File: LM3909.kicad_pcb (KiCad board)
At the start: 2 copper layers, 19 parts, among them J1 Conn_01x04, J2 Conn_01x04, Q1 MMBT3904, Q2A1 MMBT3906, Q2B1 MMBT3906, Q3 MMBT3904, Q4 MMBT3904

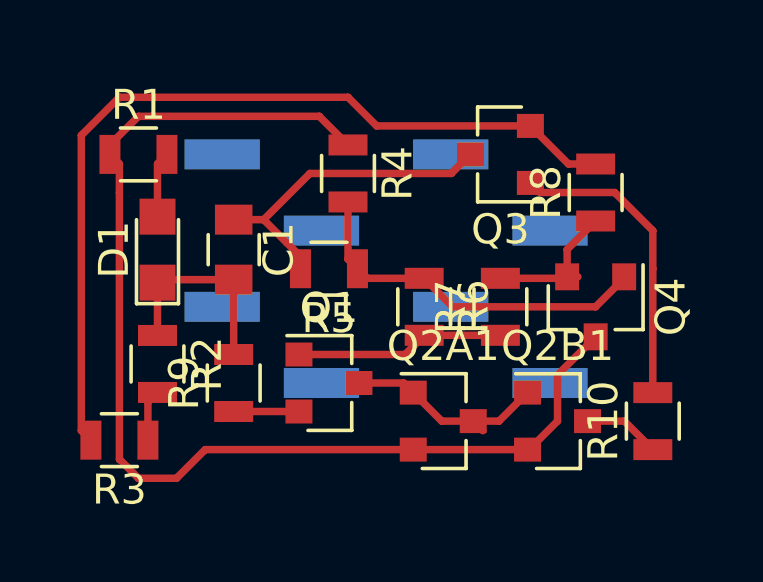
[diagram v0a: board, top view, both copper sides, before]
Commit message: connect the 6 pins on the bottom layer
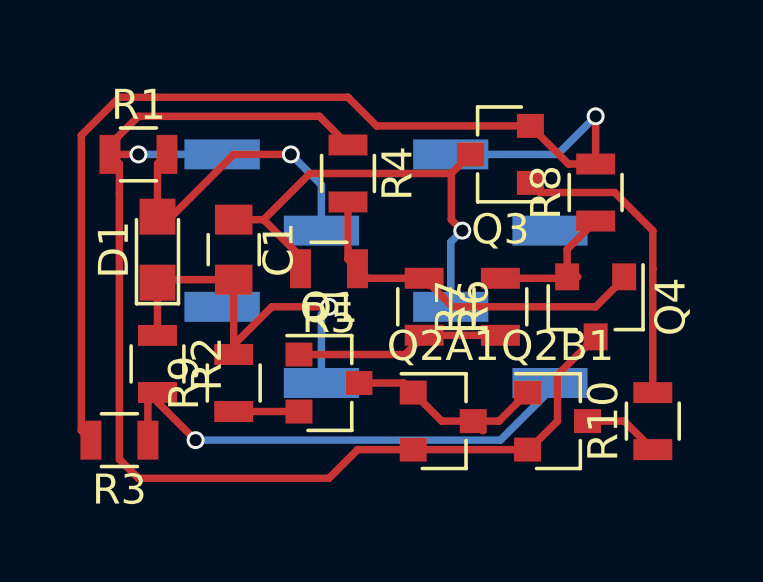
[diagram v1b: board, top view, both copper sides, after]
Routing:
- net Net-(J1-Pad1): track 1.72 -> 16.6 mm, vias 0 -> 1
- net Net-(D1-Pad2): track 2.21 -> 10.5 mm, vias 0 -> 1
- net Net-(BT1-Pad2): track 28.9 -> 35.8 mm, vias 0 -> 1
- net Net-(C1-Pad2): track 7.08 -> 13.7 mm, vias 0 -> 1
- net Net-(C1-Pad1): track 10.9 -> 15.7 mm, vias 0 -> 1
- net Net-(BT1-Pad1): track 38.4 -> 42.1 mm, vias 0 -> 1
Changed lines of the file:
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@@
   (general
     (links 32)
-    (no_connects 6)
+    (no_connects 0)
     (area 0 0 0 0)
     (thickness 1.6)
     (drawings 0)
-    (tracks 74)
+    (tracks 104)
     (zones 0)
     (modules 19)
@@
   (layers
     (0 F.Cu signal)
-    (31 B.Cu signal hide)
+    (31 B.Cu signal)
     (32 B.Adhes user hide)
     (33 F.Adhes user hide)
@@
     )
   )
+  (segment (start 132.985 109.855) (end 132.985 111.395) (width 0.25) (layer F.Cu) (net 1))
+  (segment (start 132.965 112.145) (end 132.965 114.3) (width 0.25) (layer B.Cu) (net 1))
+  (segment (start 133.35 111.76) (end 132.965 112.145) (width 0.25) (layer B.Cu) (net 1))
+  (via (at 133.35 111.76) (size 0.6) (drill 0.4) (layers F.Cu B.Cu) (net 1))
+  (segment (start 132.985 111.395) (end 133.35 111.76) (width 0.25) (layer F.Cu) (net 1))
   (segment (start 127.955 113.03) (end 127.955 112.62) (width 0.25) (layer F.Cu) (net 1))
   (segment (start 127.955 112.62) (end 126.73 111.395) (width 0.25) (layer F.Cu) (net 1))
@@
   (segment (start 128.27 109.855) (end 132.985 109.855) (width 0.25) (layer F.Cu) (net 1))
   (segment (start 126.73 111.395) (end 128.27 109.855) (width 0.25) (layer F.Cu) (net 1))
+  (segment (start 125.73 115.89) (end 125.73 115.57) (width 0.25) (layer F.Cu) (net 2))
+  (segment (start 125.73 115.57) (end 127 114.3) (width 0.25) (layer F.Cu) (net 2))
+  (segment (start 128.655 114.55) (end 128.655 116.84) (width 0.25) (layer B.Cu) (net 2))
+  (segment (start 128.905 114.3) (end 128.655 114.55) (width 0.25) (layer B.Cu) (net 2))
+  (via (at 128.905 114.3) (size 0.6) (drill 0.4) (layers F.Cu B.Cu) (net 2))
+  (segment (start 127 114.3) (end 128.905 114.3) (width 0.25) (layer F.Cu) (net 2))
   (segment (start 125.73 113.395) (end 123.29 113.395) (width 0.25) (layer F.Cu) (net 2))
   (segment (start 123.29 113.395) (end 123.19 113.495) (width 0.25) (layer F.Cu) (net 2))
@@
   (segment (start 125.63 113.495) (end 125.73 113.395) (width 0.25) (layer F.Cu) (net 2))
   (segment (start 125.73 113.395) (end 125.63 113.395) (width 0.25) (layer F.Cu) (net 2))
+  (segment (start 123.19 111.295) (end 123.655 111.295) (width 0.25) (layer F.Cu) (net 3))
+  (segment (start 123.655 111.295) (end 125.73 109.22) (width 0.25) (layer F.Cu) (net 3))
+  (segment (start 128.655 110.24) (end 128.655 111.76) (width 0.25) (layer B.Cu) (net 3))
+  (segment (start 127.635 109.22) (end 128.655 110.24) (width 0.25) (layer B.Cu) (net 3))
+  (via (at 127.635 109.22) (size 0.6) (drill 0.4) (layers F.Cu B.Cu) (net 3))
+  (segment (start 125.73 109.22) (end 127.635 109.22) (width 0.25) (layer F.Cu) (net 3))
   (segment (start 123.19 111.295) (end 123.19 109.535) (width 0.25) (layer F.Cu) (net 3))
   (segment (start 123.19 109.535) (end 123.505 109.22) (width 0.25) (layer F.Cu) (net 3))
@@
   (segment (start 127.905 115.89) (end 131.44 115.89) (width 0.25) (layer F.Cu) (net 6))
   (segment (start 131.44 115.89) (end 132.08 115.25) (width 0.25) (layer F.Cu) (net 6))
+  (segment (start 121.605 109.22) (end 122.555 109.22) (width 0.25) (layer F.Cu) (net 7) (status 400000))
+  (segment (start 122.555 109.22) (end 125.345 109.22) (width 0.25) (layer B.Cu) (net 7) (status 800000))
+  (via (at 122.555 109.22) (size 0.6) (drill 0.4) (layers F.Cu B.Cu) (net 7))
   (segment (start 135.525 119.06) (end 135.575 119.06) (width 0.25) (layer F.Cu) (net 7))
   (segment (start 135.575 119.06) (end 136.525 118.11) (width 0.25) (layer F.Cu) (net 7))
@@
   (segment (start 122.555 107.95) (end 128.585 107.95) (width 0.25) (layer F.Cu) (net 7))
   (segment (start 121.92 109.535) (end 121.92 110.49) (width 0.25) (layer F.Cu) (net 7))
-  (segment (start 124.78 119.06) (end 123.825 120.015) (width 0.25) (layer F.Cu) (net 7))
-  (segment (start 123.825 120.015) (end 122.555 120.015) (width 0.25) (layer F.Cu) (net 7))
+  (segment (start 129.86 119.06) (end 128.905 120.015) (width 0.25) (layer F.Cu) (net 7))
+  (segment (start 128.905 120.015) (end 122.555 120.015) (width 0.25) (layer F.Cu) (net 7))
   (segment (start 122.555 120.015) (end 121.92 119.38) (width 0.25) (layer F.Cu) (net 7))
   (segment (start 121.92 119.38) (end 121.92 110.49) (width 0.25) (layer F.Cu) (net 7))
-  (segment (start 124.78 119.06) (end 131.715 119.06) (width 0.25) (layer F.Cu) (net 7))
+  (segment (start 129.86 119.06) (end 131.715 119.06) (width 0.25) (layer F.Cu) (net 7) (status 800000))
   (segment (start 121.92 109.535) (end 121.605 109.22) (width 0.25) (layer F.Cu) (net 7))
   (segment (start 131.715 119.06) (end 131.715 119.11) (width 0.25) (layer F.Cu) (net 7))
   (segment (start 137.525 118.11) (end 138.75 118.11) (width 0.25) (layer F.Cu) (net 8))
   (segment (start 138.75 118.11) (end 139.7 119.06) (width 0.25) (layer F.Cu) (net 8))
+  (segment (start 132.965 109.22) (end 136.525 109.22) (width 0.25) (layer B.Cu) (net 9))
+  (segment (start 137.795 107.95) (end 137.795 109.54) (width 0.25) (layer F.Cu) (net 9))
+  (via (at 137.795 107.95) (size 0.6) (drill 0.4) (layers F.Cu B.Cu) (net 9))
+  (segment (start 136.525 109.22) (end 137.795 107.95) (width 0.25) (layer B.Cu) (net 9))
   (segment (start 135.62 108.27) (end 130.495 108.27) (width 0.25) (layer F.Cu) (net 9))
   (segment (start 120.65 108.585) (end 120.65 118.425) (width 0.25) (layer F.Cu) (net 9))
@@
   (segment (start 139.7 113.03) (end 139.7 117.16) (width 0.25) (layer F.Cu) (net 12))
   (segment (start 139.7 113.03) (end 139.7 113.03) (width 0.25) (layer F.Cu) (net 12))
+  (segment (start 123.19 117.155) (end 123.19 117.475) (width 0.25) (layer F.Cu) (net 13) (status C00000))
+  (segment (start 123.19 117.475) (end 124.46 118.745) (width 0.25) (layer F.Cu) (net 13) (status 400000))
+  (segment (start 134.62 118.745) (end 136.275 117.09) (width 0.25) (layer B.Cu) (net 13) (status 800000))
+  (segment (start 124.46 118.745) (end 134.62 118.745) (width 0.25) (layer B.Cu) (net 13))
+  (via (at 124.46 118.745) (size 0.6) (drill 0.4) (layers F.Cu B.Cu) (net 13))
+  (segment (start 136.275 117.09) (end 136.275 116.84) (width 0.25) (layer B.Cu) (net 13) (status C00000))
   (segment (start 122.87 118.745) (end 122.87 117.475) (width 0.25) (layer F.Cu) (net 13))
   (segment (start 122.87 117.475) (end 123.19 117.155) (width 0.25) (layer F.Cu) (net 13))

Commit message: add board outline
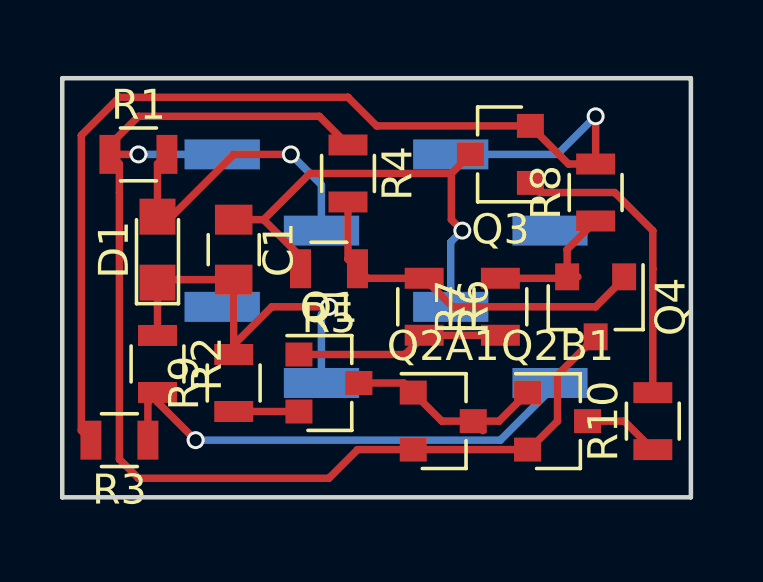
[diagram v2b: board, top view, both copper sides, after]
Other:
- board outline added: 21 x 14 mm
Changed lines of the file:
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@@
     (links 32)
     (no_connects 0)
-    (area 0 0 0 0)
+    (area 119.979524 105.695 142.575 121.735)
     (thickness 1.6)
-    (drawings 0)
+    (drawings 4)
     (tracks 104)
     (zones 0)
@@
     (42 Eco1.User user hide)
     (43 Eco2.User user hide)
-    (44 Edge.Cuts user hide)
+    (44 Edge.Cuts user)
     (45 Margin user hide)
     (46 B.CrtYd user hide)
@@
     )
   )
+  (gr_line (start 120.015 120.65) (end 120.015 106.68) (angle 90) (layer Edge.Cuts) (width 0.15))
+  (gr_line (start 140.97 120.65) (end 120.015 120.65) (angle 90) (layer Edge.Cuts) (width 0.15))
+  (gr_line (start 140.97 106.68) (end 140.97 120.65) (angle 90) (layer Edge.Cuts) (width 0.15))
+  (gr_line (start 120.015 106.68) (end 140.97 106.68) (angle 90) (layer Edge.Cuts) (width 0.15))
   (segment (start 132.985 109.855) (end 132.985 111.395) (width 0.25) (layer F.Cu) (net 1))
   (segment (start 132.965 112.145) (end 132.965 114.3) (width 0.25) (layer B.Cu) (net 1))
@@
   (segment (start 127.905 115.89) (end 131.44 115.89) (width 0.25) (layer F.Cu) (net 6))
   (segment (start 131.44 115.89) (end 132.08 115.25) (width 0.25) (layer F.Cu) (net 6))
-  (segment (start 121.605 109.22) (end 122.555 109.22) (width 0.25) (layer F.Cu) (net 7) (status 400000))
-  (segment (start 122.555 109.22) (end 125.345 109.22) (width 0.25) (layer B.Cu) (net 7) (status 800000))
+  (segment (start 121.605 109.22) (end 122.555 109.22) (width 0.25) (layer F.Cu) (net 7))
+  (segment (start 122.555 109.22) (end 125.345 109.22) (width 0.25) (layer B.Cu) (net 7))
   (via (at 122.555 109.22) (size 0.6) (drill 0.4) (layers F.Cu B.Cu) (net 7))
   (segment (start 135.525 119.06) (end 135.575 119.06) (width 0.25) (layer F.Cu) (net 7))
@@
   (segment (start 122.555 120.015) (end 121.92 119.38) (width 0.25) (layer F.Cu) (net 7))
   (segment (start 121.92 119.38) (end 121.92 110.49) (width 0.25) (layer F.Cu) (net 7))
-  (segment (start 129.86 119.06) (end 131.715 119.06) (width 0.25) (layer F.Cu) (net 7) (status 800000))
+  (segment (start 129.86 119.06) (end 131.715 119.06) (width 0.25) (layer F.Cu) (net 7))
   (segment (start 121.92 109.535) (end 121.605 109.22) (width 0.25) (layer F.Cu) (net 7))
   (segment (start 131.715 119.06) (end 131.715 119.11) (width 0.25) (layer F.Cu) (net 7))
@@
   (segment (start 139.7 113.03) (end 139.7 117.16) (width 0.25) (layer F.Cu) (net 12))
   (segment (start 139.7 113.03) (end 139.7 113.03) (width 0.25) (layer F.Cu) (net 12))
-  (segment (start 123.19 117.155) (end 123.19 117.475) (width 0.25) (layer F.Cu) (net 13) (status C00000))
-  (segment (start 123.19 117.475) (end 124.46 118.745) (width 0.25) (layer F.Cu) (net 13) (status 400000))
-  (segment (start 134.62 118.745) (end 136.275 117.09) (width 0.25) (layer B.Cu) (net 13) (status 800000))
+  (segment (start 123.19 117.155) (end 123.19 117.475) (width 0.25) (layer F.Cu) (net 13))
+  (segment (start 123.19 117.475) (end 124.46 118.745) (width 0.25) (layer F.Cu) (net 13))
+  (segment (start 134.62 118.745) (end 136.275 117.09) (width 0.25) (layer B.Cu) (net 13))
   (segment (start 124.46 118.745) (end 134.62 118.745) (width 0.25) (layer B.Cu) (net 13))
   (via (at 124.46 118.745) (size 0.6) (drill 0.4) (layers F.Cu B.Cu) (net 13))
-  (segment (start 136.275 117.09) (end 136.275 116.84) (width 0.25) (layer B.Cu) (net 13) (status C00000))
+  (segment (start 136.275 117.09) (end 136.275 116.84) (width 0.25) (layer B.Cu) (net 13))
   (segment (start 122.87 118.745) (end 122.87 117.475) (width 0.25) (layer F.Cu) (net 13))
   (segment (start 122.87 117.475) (end 123.19 117.155) (width 0.25) (layer F.Cu) (net 13))

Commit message: move silkscreen into place
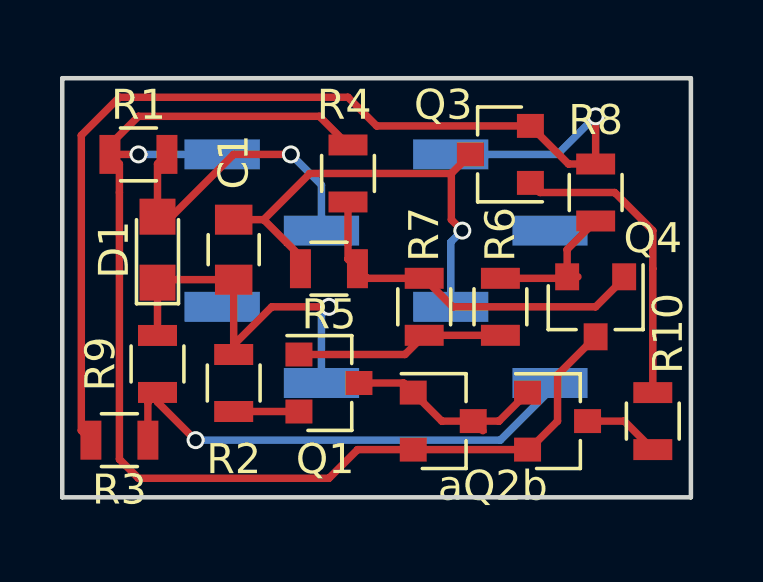
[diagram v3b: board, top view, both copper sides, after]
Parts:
- renumbered Q2A1 to aQ2b
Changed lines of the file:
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@@
     (links 32)
     (no_connects 0)
-    (area 119.979524 105.695 142.575 121.735)
+    (area 119.939999 105.695 142.575 123.045)
     (thickness 1.6)
     (drawings 4)
@@
   (layers
     (0 F.Cu signal)
-    (31 B.Cu signal)
+    (31 B.Cu signal hide)
     (32 B.Adhes user hide)
     (33 F.Adhes user hide)
     (34 B.Paste user hide)
     (35 F.Paste user hide)
-    (36 B.SilkS user hide)
+    (36 B.SilkS user)
     (37 F.SilkS user)
     (38 B.Mask user hide)
@@
     (47 F.CrtYd user)
     (48 B.Fab user hide)
-    (49 F.Fab user)
+    (49 F.Fab user hide)
   )
   (setup
@@
     (pad_to_mask_clearance 0.2)
     (aux_axis_origin 0 0)
-    (visible_elements 7FFFFF9F)
+    (visible_elements 7FFFFFBF)
     (pcbplotparams
-      (layerselection 0x00030_80000001)
+      (layerselection 0x000f0_80000001)
       (usegerberextensions false)
       (excludeedgelayer true)
@@
       (outputformat 1)
       (mirror false)
-      (drillshape 1)
+      (drillshape 0)
       (scaleselection 1)
-      (outputdirectory ""))
+      (outputdirectory GerberFiles/))
   )
   (net 0 "")
@@
     (tags "resistor 0805")
     (attr smd)
-    (fp_text reference R2 (at 0 -1.65 270) (layer F.SilkS)
+    (fp_text reference R2 (at 3.175 -2.54 360) (layer F.SilkS)
       (effects (font (size 1 1) (thickness 0.15)))
     )
@@
     (tags "capacitor 0805")
     (attr smd)
-    (fp_text reference C1 (at 0 -1.5 270) (layer F.SilkS)
+    (fp_text reference C1 (at -2.921 0 270) (layer F.SilkS)
       (effects (font (size 1 1) (thickness 0.15)))
     )
@@
     (tags "resistor 0805")
     (attr smd)
-    (fp_text reference R4 (at 0 -1.65 270) (layer F.SilkS)
+    (fp_text reference R4 (at -2.286 0.127 360) (layer F.SilkS)
       (effects (font (size 1 1) (thickness 0.15)))
     )
@@
     (tags "resistor 0805")
     (attr smd)
-    (fp_text reference R5 (at 0 -1.65 180) (layer F.SilkS)
+    (fp_text reference R5 (at 0 -1.524 180) (layer F.SilkS)
       (effects (font (size 1 1) (thickness 0.15)))
     )
@@
     (tags "resistor 0805")
     (attr smd)
-    (fp_text reference R6 (at 0 -1.65 270) (layer F.SilkS)
+    (fp_text reference R6 (at -2.413 -2.54 270) (layer F.SilkS)
       (effects (font (size 1 1) (thickness 0.15)))
     )
@@
     (tags "resistor 0805")
     (attr smd)
-    (fp_text reference R7 (at 0 -1.65 90) (layer F.SilkS)
+    (fp_text reference R7 (at 2.413 -2.54 90) (layer F.SilkS)
       (effects (font (size 1 1) (thickness 0.15)))
     )
@@
     (tags "resistor 0805")
     (attr smd)
-    (fp_text reference R8 (at 0 -1.65 90) (layer F.SilkS)
+    (fp_text reference R8 (at 2.413 0 180) (layer F.SilkS)
       (effects (font (size 1 1) (thickness 0.15)))
     )
@@
     (tags "resistor 0805")
     (attr smd)
-    (fp_text reference R9 (at 0 -1.65 90) (layer F.SilkS)
+    (fp_text reference R9 (at 0.635 -4.445 90) (layer F.SilkS)
       (effects (font (size 1 1) (thickness 0.15)))
     )
@@
     (tags SOT-23)
     (attr smd)
-    (fp_text reference Q1 (at 0 -2.5) (layer F.SilkS)
+    (fp_text reference Q1 (at -0.127 2.54) (layer F.SilkS)
       (effects (font (size 1 1) (thickness 0.15)))
     )
@@
     (tags SOT-23)
     (attr smd)
-    (fp_text reference Q2A1 (at 0 -2.5) (layer F.SilkS)
+    (fp_text reference aQ2b (at 1.651 2.159) (layer F.SilkS)
       (effects (font (size 1 1) (thickness 0.15)))
     )
@@
     (tags SOT-23)
     (attr smd)
-    (fp_text reference Q2B1 (at 0 -2.5) (layer F.SilkS)
+    (fp_text reference Q2B1 (at -0.254 3.81) (layer F.SilkS) hide
       (effects (font (size 1 1) (thickness 0.15)))
     )
@@
     (tags SOT-23)
     (attr smd)
-    (fp_text reference Q3 (at 0 -2.5 180) (layer F.SilkS)
+    (fp_text reference Q3 (at 1.905 1.651 180) (layer F.SilkS)
       (effects (font (size 1 1) (thickness 0.15)))
     )
@@
     (tags SOT-23)
     (attr smd)
-    (fp_text reference Q4 (at 0 -2.5 270) (layer F.SilkS)
+    (fp_text reference Q4 (at -2.286 -1.905 360) (layer F.SilkS)
       (effects (font (size 1 1) (thickness 0.15)))
     )
@@
     (tags "resistor 0805")
     (attr smd)
-    (fp_text reference R10 (at 0 -1.65 90) (layer F.SilkS)
-      (effects (font (size 1 1) (thickness 0.15)))
-    )
+    (fp_text reference R10 (at 2.921 0.508 90) (layer F.SilkS)
+      (effects (font (size 1 1) (thickness 0.15)))
+    )
